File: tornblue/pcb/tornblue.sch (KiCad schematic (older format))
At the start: 78 parts, among them J1 BATT, J2 SWD, J3 BREAKOUT, J4 USB C - USB2.0, Q1 AO3401A, Q2 AO3401A, SW1 SW_Push, SW10 SW_Push, SW11 SW_Push, SW12 SW_Push, SW13 SW_Push, SW14 SW_Push, SW15 SW_Push, SW16 SW_Push, SW17 SW_Push, SW18 SW_Push, SW19 EC11, SW2 SW_Push, SW20 SW_Push, SW21 SW_Push, SW22 EC11, SW23 RESET, SW3 SW_Push, SW4 SW_Push, SW5 SW_Push, SW6 SW_Push, SW7 SW_Push, SW8 SW_Push, SW9 SW_Push, U1 XC6220, U2 TP4056, U3 nRF52840_holyiot_18010, U4 SRV05-4

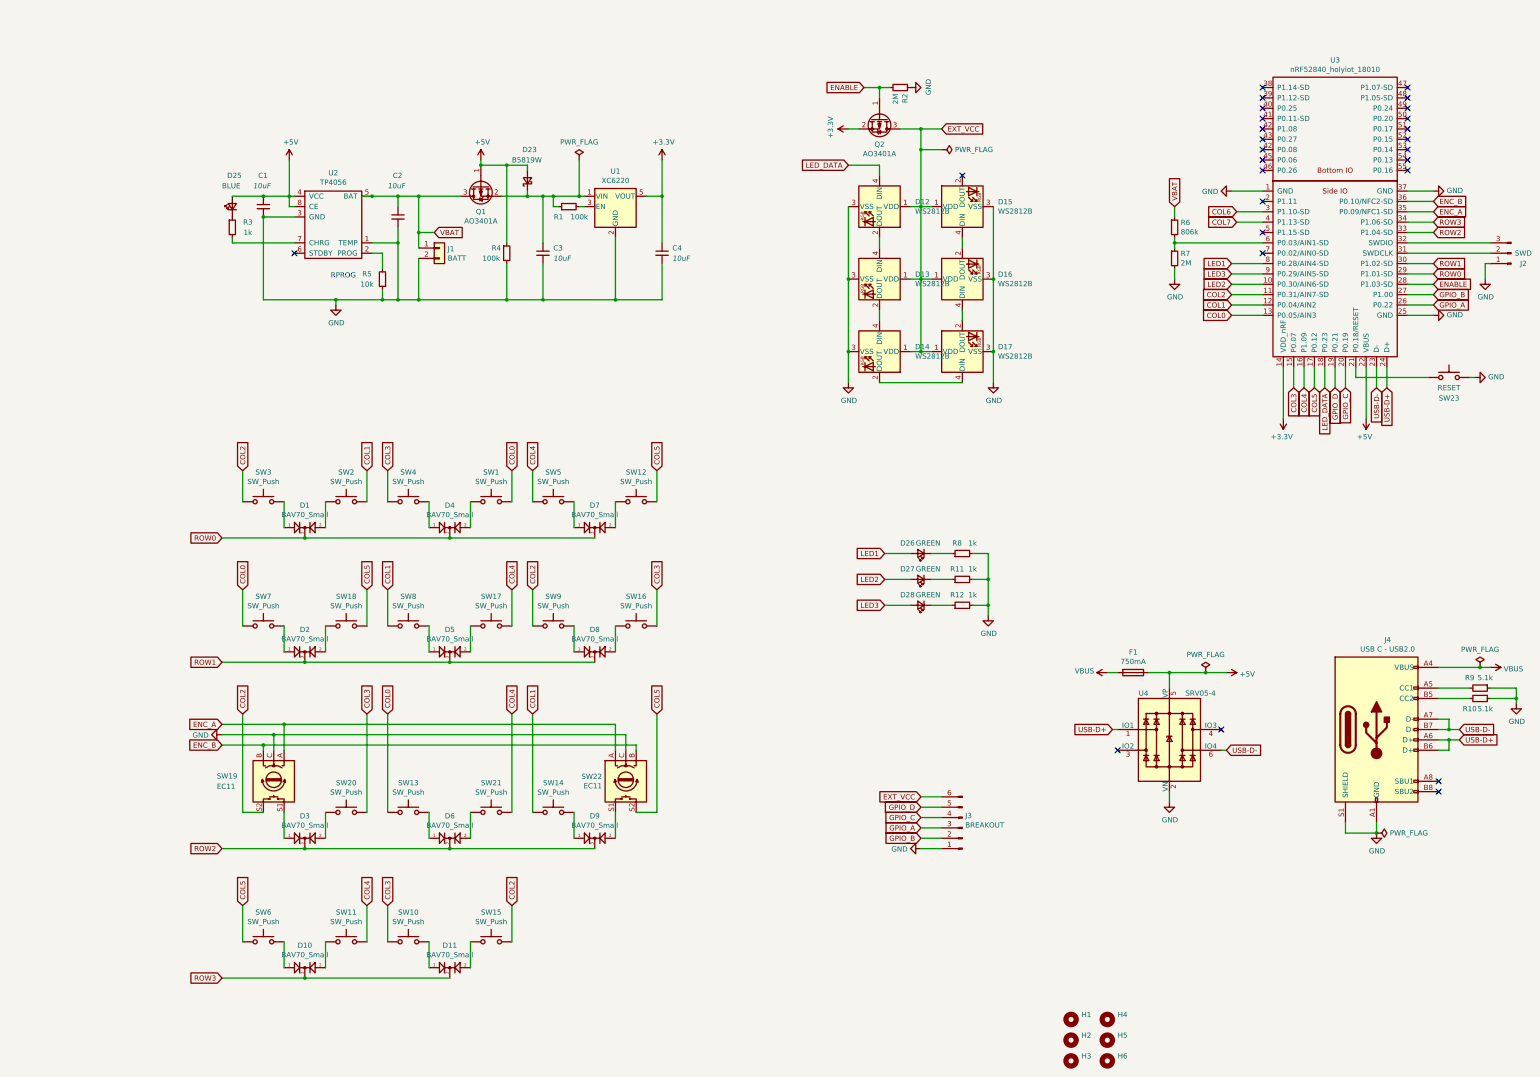
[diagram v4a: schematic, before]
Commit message: Add battery pins + silk screen fixes
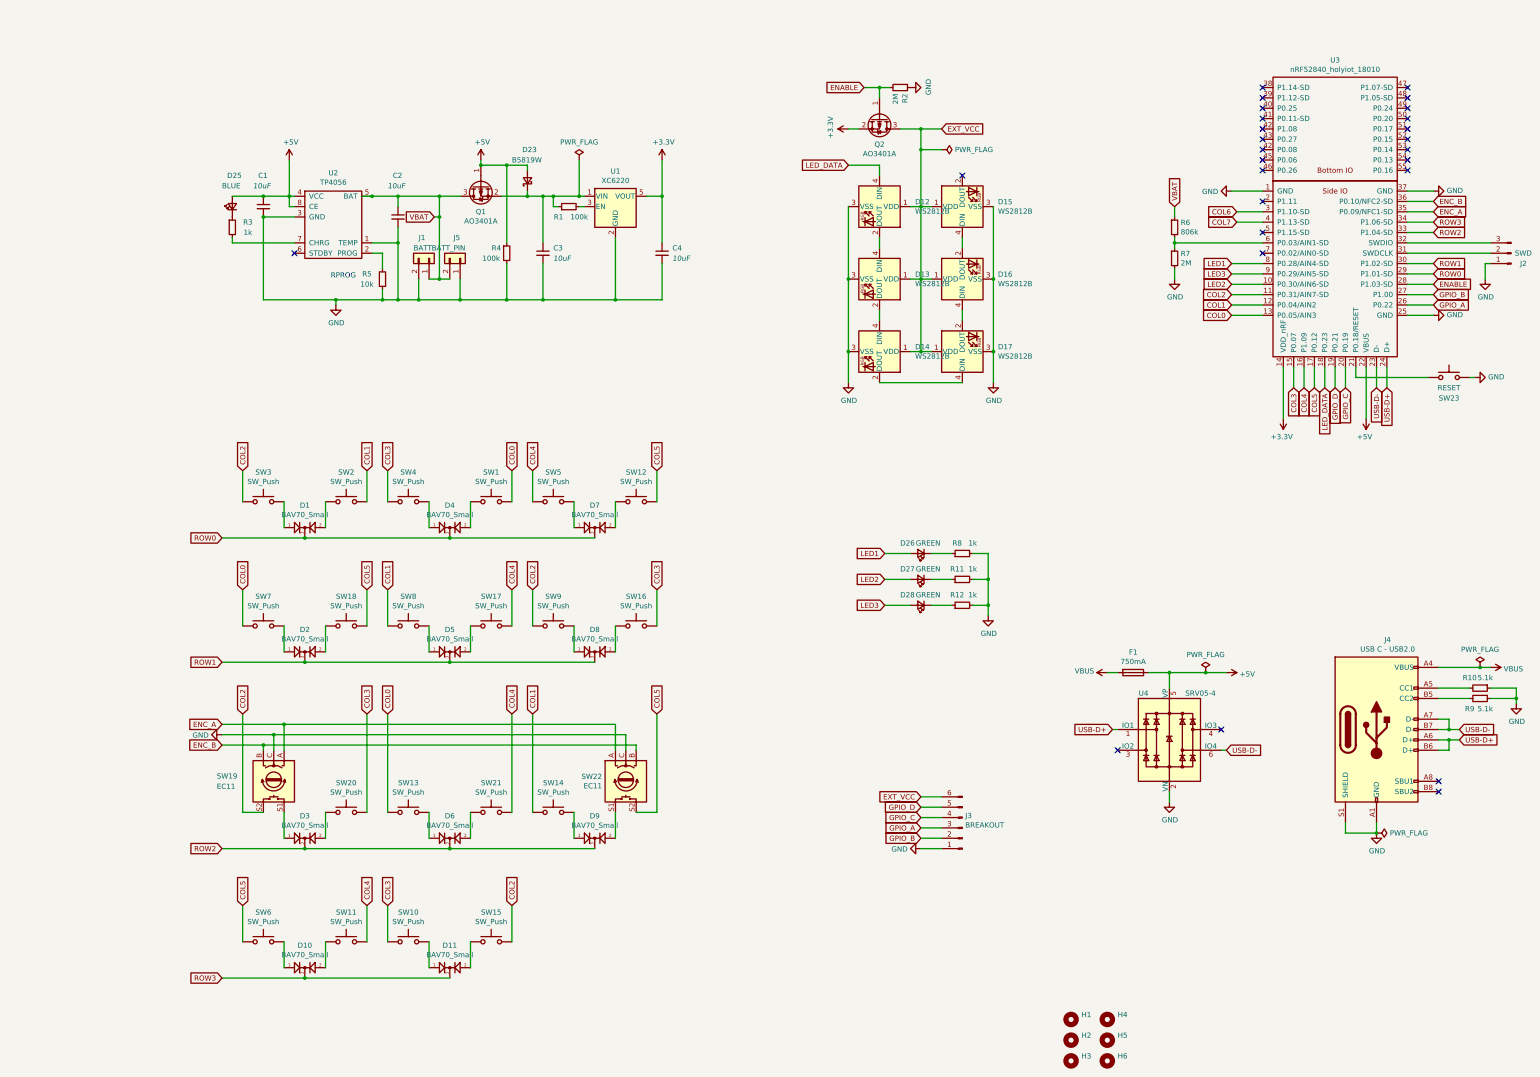
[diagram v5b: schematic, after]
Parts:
- added J5: BATT_PIN, Connector_PinHeader_2.54mm:PinHeader_1x02_P2.54mm_Vertical, symbol Connector_Generic:Conn_01x02
- renumbered R9 to R10, R10 to R9
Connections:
- net GND: now also J5.1 (Pin_1)
- net VBAT: now also J5.2 (Pin_2)
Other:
- moved on the sheet: J1
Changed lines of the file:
@@
 	0    1    1    0
 $EndComp
-$Comp
-L Connector_Generic:Conn_01x02 J1
-U 1 1 61143221
-P 4850 2950
-F 0 "J1" H 4930 2942 50  0000 L CNN
-F 1 "BATT" H 4930 2851 50  0000 L CNN
-F 2 "Connector_JST:JST_PH_S2B-PH-SM4-TB_1x02-1MP_P2.00mm_Horizontal" H 4850 2950 50  0001 C CNN
-F 3 "~" H 4850 2950 50  0001 C CNN
-F 4 "-" H 4850 2950 50  0001 C CNN "LCSC"
-	1    4850 2950
-	1    0    0    -1
-$EndComp
 Wire Wire Line
 	15000 3100 14950 3100
-Text GLabel 4800 2800 2    50   Input ~ 0
+Text GLabel 4800 2650 0    50   Input ~ 0
 VBAT
 $Comp
@@
 Wire Wire Line
 	4200 3000 4300 3000
-Wire Wire Line
-	4650 2450 4650 2800
 $Comp
 L power:+5V #PWR01
@@
 Wire Wire Line
 	3400 2550 3450 2550
-Connection ~ 4650 2450
 Connection ~ 4450 2450
 Wire Wire Line
@@
 	4100 2450 4200 2450
 Wire Wire Line
-	4450 2450 4650 2450
-Wire Wire Line
 	3850 3450 4300 3450
 Connection ~ 3850 3450
@@
 Wire Wire Line
 	13400 4300 13400 4100
-Wire Wire Line
-	4450 3450 4650 3450
-Wire Wire Line
-	4650 3050 4650 3450
 $Comp
 L Device:D_Schottky_Small D23
@@
 $EndComp
 Wire Wire Line
-	4800 2800 4650 2800
-Wire Wire Line
-	4650 2450 5050 2450
-Connection ~ 4650 2800
-Wire Wire Line
-	4650 2800 4650 2950
-Wire Wire Line
 	5500 2900 5500 2150
 Wire Wire Line
-	4650 3450 5500 3450
-Wire Wire Line
 	5500 3450 5500 3100
-Connection ~ 4650 3450
 Wire Wire Line
 	6250 2550 6200 2550
@@
 NoConn ~ 14500 8100
 $Comp
-L Device:R_Small R10
+L Device:R_Small R9
 U 1 1 610FC56D
 P 14900 7300
-F 0 "R10" V 15000 7200 50  0000 C CNN
+F 0 "R9" V 15000 7200 50  0000 C CNN
 F 1 "5.1k" V 15000 7350 50  0000 C CNN
 F 2 "Resistor_SMD:R_0805_2012Metric" H 14900 7300 50  0001 C CNN
@@
 $EndComp
 $Comp
-L Device:R_Small R9
+L Device:R_Small R10
 U 1 1 610FB86F
 P 14900 7200
-F 0 "R9" V 14800 7100 50  0000 C CNN
+F 0 "R10" V 14800 7100 50  0000 C CNN
 F 1 "5.1k" V 14800 7250 50  0000 C CNN
 F 2 "Resistor_SMD:R_0805_2012Metric" H 14900 7200 50  0001 C CNN
@@
 Text GLabel 2950 6250 1    50   Input ~ 0
 COL0
+$Comp
+L Connector_Generic:Conn_01x02 J5
+U 1 1 6380E79A
+P 5050 3050
+F 0 "J5" V 5250 3050 50  0000 R CNN
+F 1 "BATT_PIN" V 5150 3100 50  0000 R CNN
+F 2 "Connector_PinHeader_2.54mm:PinHeader_1x02_P2.54mm_Vertical" H 5050 3050 50  0001 C CNN
+F 3 "~" H 5050 3050 50  0001 C CNN
+	1    5050 3050
+	0    1    -1   0
+$EndComp
+Wire Wire Line
+	4450 3450 4650 3450
+$Comp
+L Connector_Generic:Conn_01x02 J1
+U 1 1 61143221
+P 4750 3050
+F 0 "J1" V 4950 2950 50  0000 L CNN
+F 1 "BATT" V 4850 2900 50  0000 L CNN
+F 2 "Connector_JST:JST_PH_S2B-PH-SM4-TB_1x02-1MP_P2.00mm_Horizontal" H 4750 3050 50  0001 C CNN
+F 3 "~" H 4750 3050 50  0001 C CNN
+F 4 "-" H 4750 3050 50  0001 C CNN "LCSC"
+	1    4750 3050
+	0    1    -1   0
+$EndComp
+Wire Wire Line
+	4650 3250 4650 3450
+Connection ~ 4650 3450
+Wire Wire Line
+	4650 3450 5050 3450
+Wire Wire Line
+	5050 3250 5050 3450
+Connection ~ 5050 3450
+Wire Wire Line
+	5050 3450 5500 3450
+Wire Wire Line
+	4950 3250 4850 3250
+Connection ~ 4850 3250
+Wire Wire Line
+	4850 3250 4750 3250
+Connection ~ 4850 2450
+Wire Wire Line
+	4850 2450 5050 2450
+Wire Wire Line
+	4800 2650 4850 2650
+Wire Wire Line
+	4450 2450 4850 2450
+Connection ~ 4850 2650
+Wire Wire Line
+	4850 2650 4850 2450
+Wire Wire Line
+	4850 2650 4850 3250
 $EndSCHEMATC

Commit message: Add power switch
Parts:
- added SW24: SW_SPST, Button_Switch_SMD:SW_SPDT_PCM12, symbol Switch:SW_Push_SPDT
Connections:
- net +3V3: now also SW24.1 (A); no longer C4.1, U1.5 (VOUT)
- net COL6: no longer names the net of U3.3 (P1.10-SD)
- net COL7: no longer names the net of U3.4 (P1.13-SD)
- new net: C4.1, SW24.2 (B), U1.5 (VOUT)
- no-connect marks 27 -> 30
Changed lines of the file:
@@
 L power:+3.3V #PWR03
 U 1 1 636864E2
-P 7000 2100
-F 0 "#PWR03" H 7000 1950 50  0001 C CNN
-F 1 "+3.3V" H 7015 2273 50  0000 C CNN
-F 2 "" H 7000 2100 50  0001 C CNN
-F 3 "" H 7000 2100 50  0001 C CNN
-	1    7000 2100
-	1    0    0    -1
+P 7600 2350
+F 0 "#PWR03" H 7600 2200 50  0001 C CNN
+F 1 "+3.3V" H 7615 2523 50  0000 C CNN
+F 2 "" H 7600 2350 50  0001 C CNN
+F 3 "" H 7600 2350 50  0001 C CNN
+	1    7600 2350
+	0    1    1    0
 $EndComp
 $Comp
@@
 	7000 2450 6850 2450
 Wire Wire Line
-	7000 2450 7000 2100
-Connection ~ 7000 2450
-Wire Wire Line
 	5950 2550 6000 2550
 Wire Wire Line
@@
 	1    0    0    -1
 $EndComp
-Text GLabel 12550 2600 0    50   Input ~ 0
-COL6
-Text GLabel 12550 2700 0    50   Input ~ 0
-COL7
-Wire Wire Line
-	12550 2600 12800 2600
-Wire Wire Line
-	12550 2700 12800 2700
 Text GLabel 5550 9300 1    50   Input ~ 0
 COL2
@@
 Wire Wire Line
 	4850 2650 4850 3250
+$Comp
+L Switch:SW_Push_SPDT SW24
+U 1 1 63A6CB29
+P 7300 2450
+F 0 "SW24" H 7300 2125 50  0000 C CNN
+F 1 "SW_SPST" H 7300 2216 50  0000 C CNN
+F 2 "Button_Switch_SMD:SW_SPDT_PCM12" H 7300 2450 50  0001 C CNN
+F 3 "~" H 7300 2450 50  0001 C CNN
+	1    7300 2450
+	1    0    0    -1
+$EndComp
+Wire Wire Line
+	7100 2450 7000 2450
+Connection ~ 7000 2450
+Wire Wire Line
+	7500 2350 7550 2350
+NoConn ~ 7500 2550
+NoConn ~ 12800 2600
+NoConn ~ 12800 2700
+$Comp
+L power:PWR_FLAG #FLG0103
+U 1 1 63B16A3B
+P 7550 2100
+F 0 "#FLG0103" H 7550 2175 50  0001 C CNN
+F 1 "PWR_FLAG" H 7550 2273 50  0000 C CNN
+F 2 "" H 7550 2100 50  0001 C CNN
+F 3 "~" H 7550 2100 50  0001 C CNN
+	1    7550 2100
+	1    0    0    -1
+$EndComp
+Wire Wire Line
+	7550 2100 7550 2350
+Connection ~ 7550 2350
+Wire Wire Line
+	7550 2350 7600 2350
 $EndSCHEMATC
